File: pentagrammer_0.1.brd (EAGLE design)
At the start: 46 x 21.5 mm, 20 parts, among them CON1 AVR-ISP-6, IC1 AT90S2313P

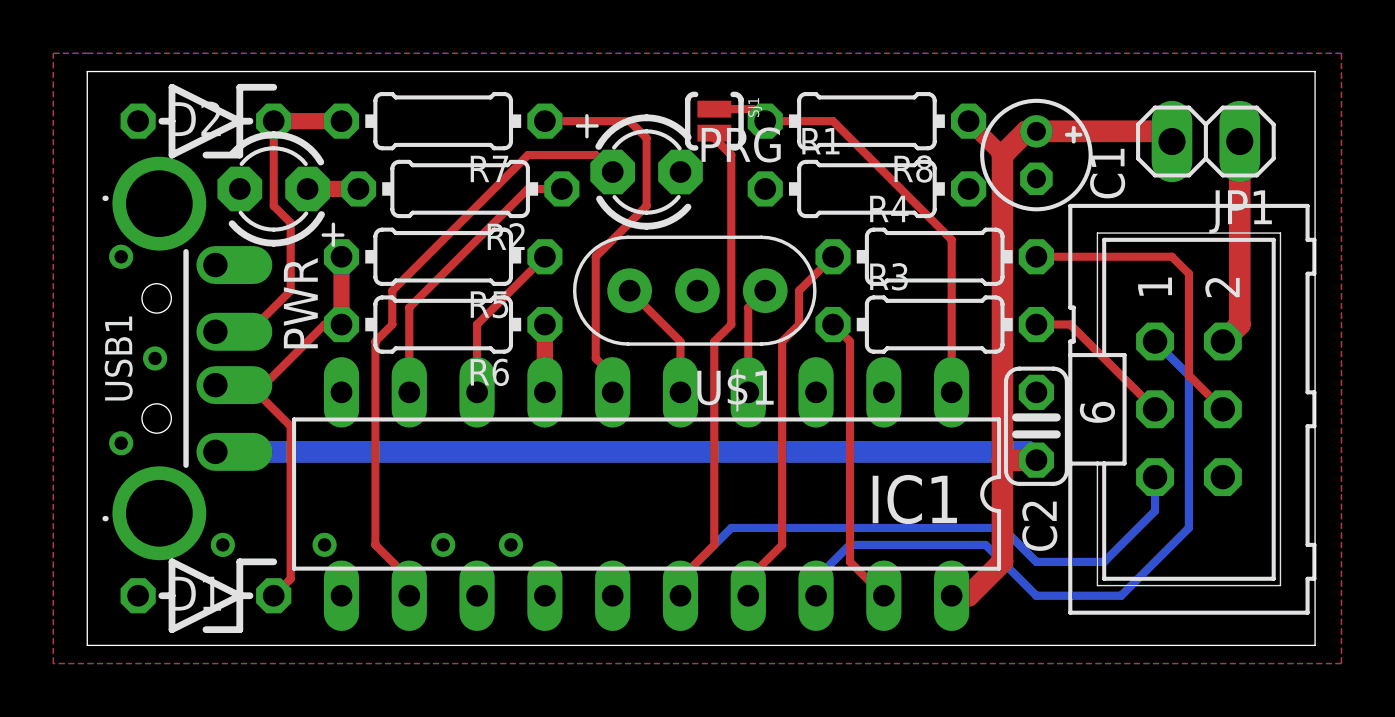
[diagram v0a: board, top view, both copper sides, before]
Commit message: added values for resistors
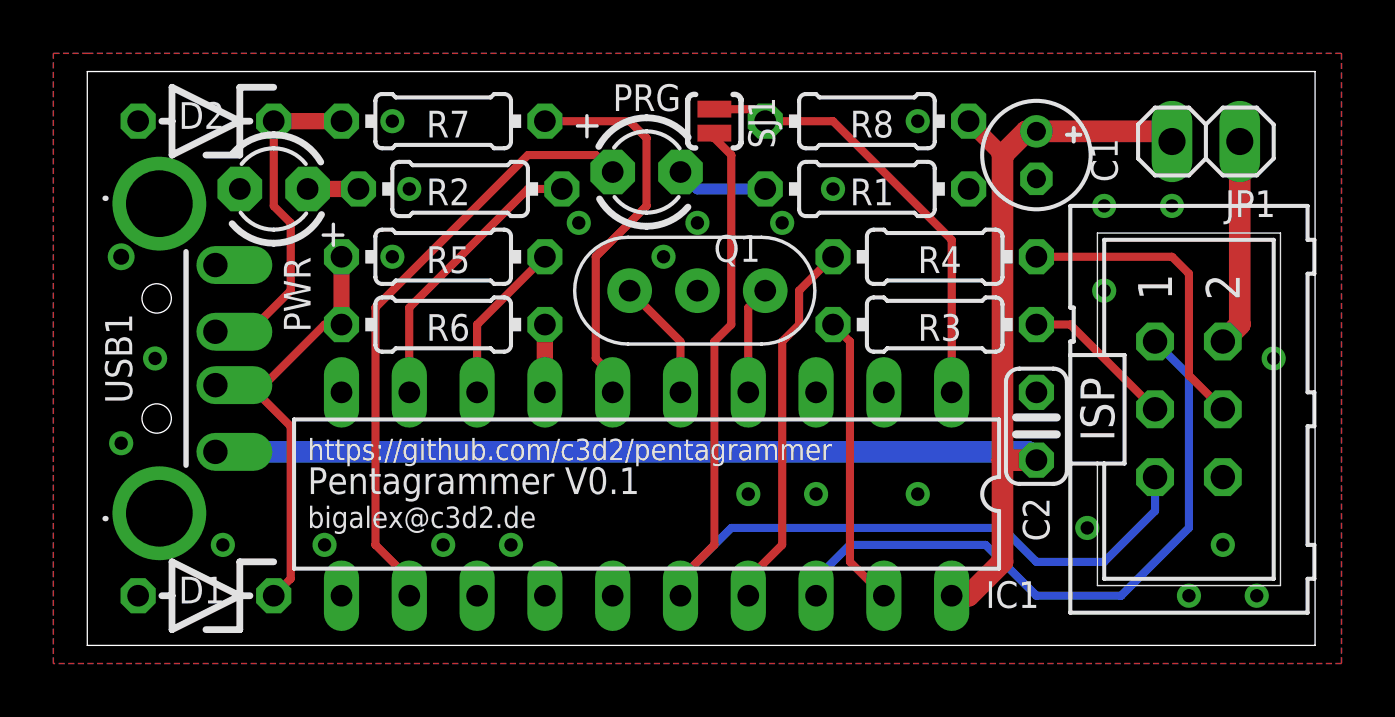
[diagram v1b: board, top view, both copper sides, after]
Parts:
- C1: value (none) -> 1u
- C2: value (none) -> 100n
- R1, R2, R3, R4: value (none) -> 1K
- R5: value (none) -> 2K2
- R6, R7: value (none) -> 68R
- R8: value (none) -> 10K
- renumbered U$1 to Q1
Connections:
- new net N$15: PRG.K, R1.1
- net GND: now also R1.2; no longer PRG.K
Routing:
- net N$15: track 0.00 -> 3.44 mm
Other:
- board text added: "Pentagrammer V0.1"
- board text added: "bigalex@c3d2.de"
- board text added: "https://github.com/c3d2/pentagrammer"
